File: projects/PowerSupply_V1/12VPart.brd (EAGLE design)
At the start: 50 x 50 mm, 26 parts, among them IC1 LM2596T, IC2 LM2596T, X1 IN, X2 OUT

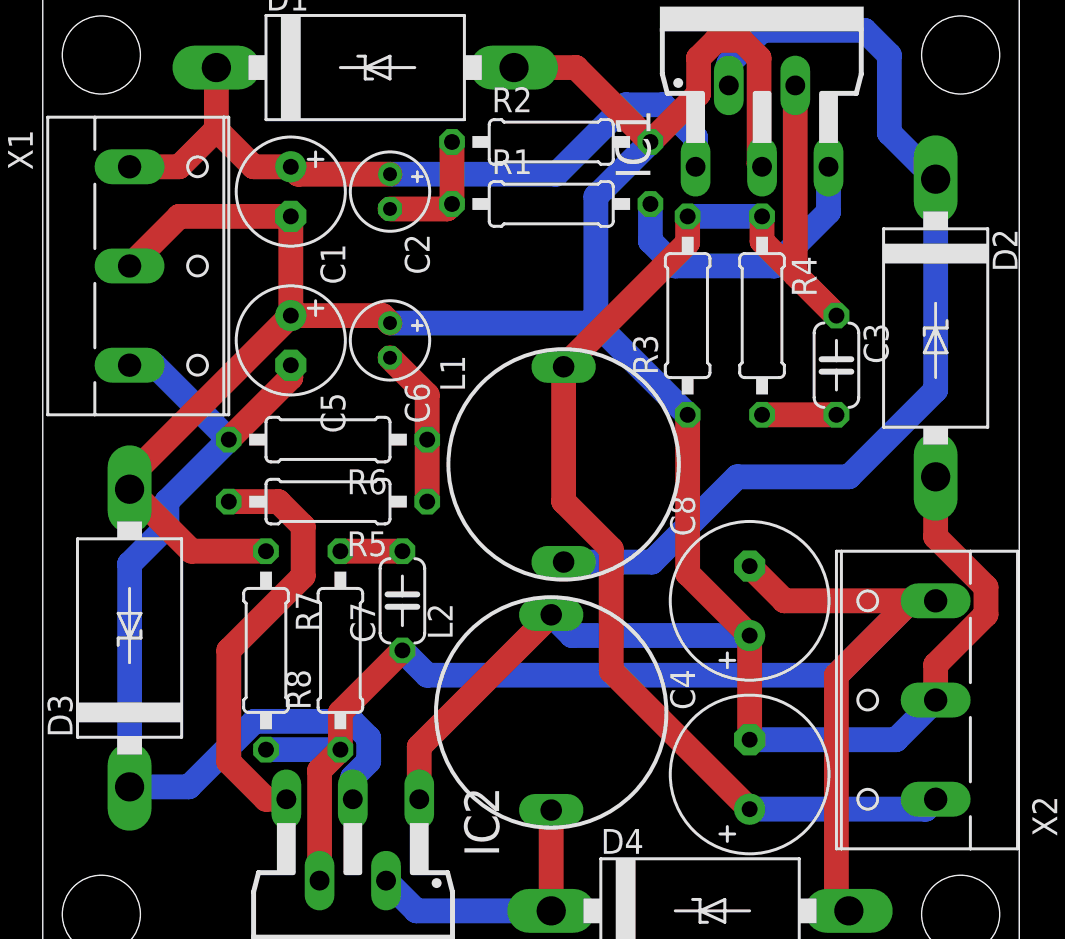
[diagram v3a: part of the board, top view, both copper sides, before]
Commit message: feat: 12VPart refactored
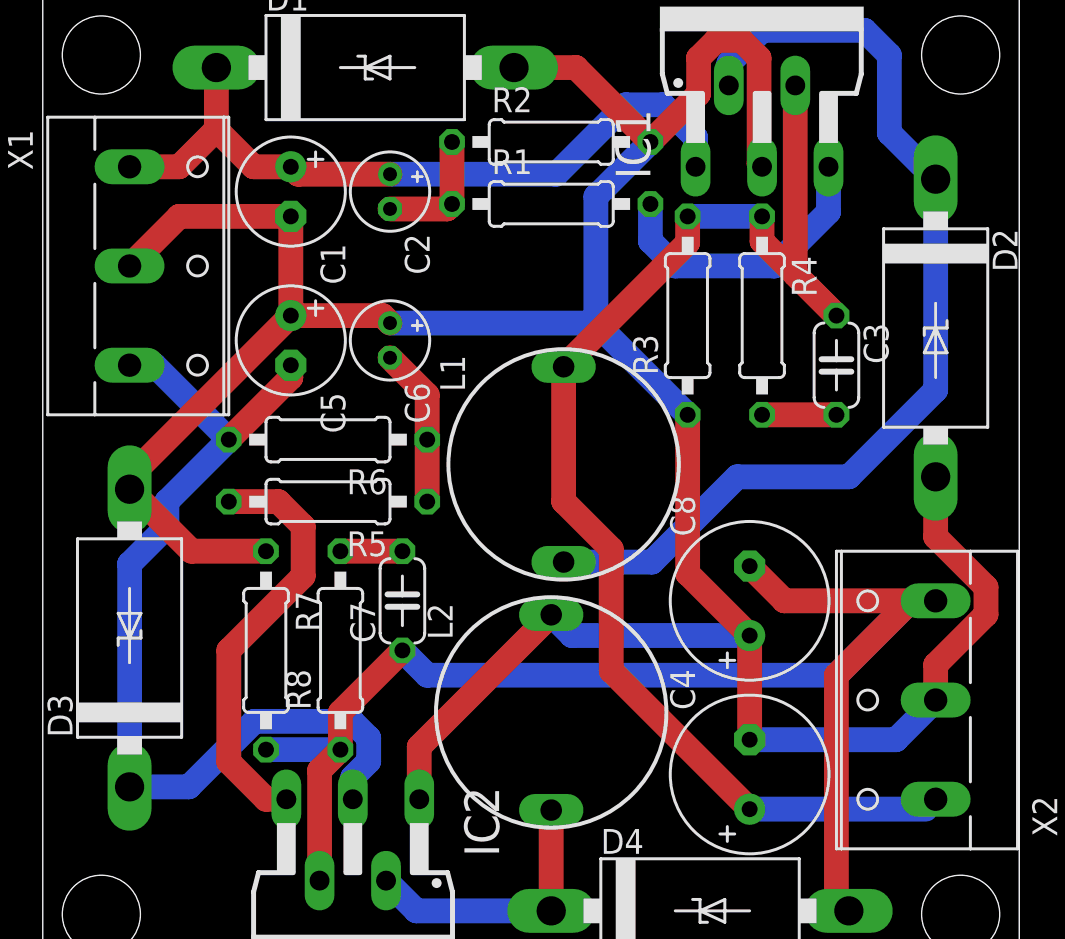
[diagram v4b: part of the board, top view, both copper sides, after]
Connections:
- net +24V renamed +20V
- net -24V renamed -20V
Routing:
- net -12V: track 76.0 -> 74.7 mm
- net +12V: track 69.8 -> 69.1 mm
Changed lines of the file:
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@@
 <wire x1="36.83" y1="28.575" x2="40.64" y2="28.575" width="1.27" layer="1"/>
-</signal>
-<signal name="+24V">
-<contactref element="X1" pad="1"/>
-<contactref element="C1" pad="+"/>
-<contactref element="IC1" pad="1"/>
-<contactref element="C2" pad="+"/>
-<contactref element="D1" pad="C"/>
-<wire x1="8.89" y1="45.72" x2="8.89" y2="46.355" width="1.27" layer="1"/>
-<wire x1="8.89" y1="43.18" x2="10.795" y2="41.275" width="1.27" layer="1"/>
-<wire x1="10.795" y1="41.275" x2="12.7" y2="41.275" width="1.27" layer="1"/>
-<wire x1="8.89" y1="46.355" x2="8.89" y2="43.18" width="1.27" layer="1"/>
-<wire x1="4.445" y1="41.275" x2="6.985" y2="41.275" width="1.27" layer="1"/>
-<wire x1="6.985" y1="41.275" x2="8.89" y2="43.18" width="1.27" layer="1"/>
-<wire x1="17.78" y1="40.894" x2="13.081" y2="40.894" width="1.27" layer="1"/>
-<wire x1="13.081" y1="40.894" x2="12.7" y2="41.275" width="1.27" layer="1"/>
-<wire x1="17.78" y1="40.894" x2="26.289" y2="40.894" width="1.27" layer="16"/>
-<wire x1="26.289" y1="40.894" x2="29.845" y2="44.45" width="1.27" layer="16"/>
-<wire x1="29.845" y1="44.45" x2="31.75" y2="44.45" width="1.27" layer="16"/>
-<wire x1="31.75" y1="44.45" x2="33.4264" y2="42.7736" width="1.27" layer="16"/>
-<wire x1="33.4264" y1="42.7736" x2="33.4264" y2="41.275" width="1.27" layer="16"/>
-</signal>
-<signal name="-24V">
-<contactref element="C5" pad="-"/>
-<contactref element="R6" pad="2"/>
-<contactref element="IC2" pad="3"/>
-<contactref element="D3" pad="C"/>
-<contactref element="X1" pad="3"/>
-<wire x1="9.525" y1="27.305" x2="12.7" y2="30.48" width="1.27" layer="1"/>
-<wire x1="12.7" y1="30.48" x2="12.7" y2="31.115" width="1.27" layer="1"/>
-<wire x1="16.6878" y1="10.8303" x2="16.6878" y2="12.0297" width="1.27" layer="16"/>
-<wire x1="16.6878" y1="12.0297" x2="15.8397" y2="12.8778" width="1.27" layer="16"/>
-<wire x1="7.4775" y1="9.525" x2="4.445" y2="9.525" width="1.27" layer="16"/>
-<wire x1="15.8397" y1="12.8778" x2="10.8303" y2="12.8778" width="1.27" layer="16"/>
-<wire x1="10.8303" y1="12.8778" x2="7.4775" y2="9.525" width="1.27" layer="16"/>
-<wire x1="15.875" y1="8.89" x2="15.875" y2="10.0175" width="1.27" layer="16"/>
-<wire x1="15.875" y1="10.0175" x2="16.6878" y2="10.8303" width="1.27" layer="16"/>
-<wire x1="4.445" y1="31.115" x2="5.715" y2="31.115" width="1.27" layer="16"/>
-<wire x1="5.715" y1="31.115" x2="9.525" y2="27.305" width="1.27" layer="16"/>
-<wire x1="9.525" y1="27.305" x2="6.35635" y2="24.13635" width="1.27" layer="16"/>
-<wire x1="6.35635" y1="24.13635" x2="6.35635" y2="22.8493375" width="1.27" layer="16"/>
-<wire x1="4.445" y1="20.9379875" x2="4.445" y2="9.525" width="1.27" layer="16"/>
-<wire x1="6.35635" y1="22.8493375" x2="4.445" y2="20.9379875" width="1.27" layer="16"/>
 </signal>
 <signal name="N$4">
@@
 <wire x1="19.685" y1="29.591" x2="19.685" y2="27.305" width="1.27" layer="1"/>
 </signal>
+<signal name="+20V">
+<contactref element="X1" pad="1"/>
+<contactref element="C1" pad="+"/>
+<contactref element="IC1" pad="1"/>
+<contactref element="C2" pad="+"/>
+<contactref element="D1" pad="C"/>
+<wire x1="8.89" y1="45.72" x2="8.89" y2="46.355" width="1.27" layer="1"/>
+<wire x1="8.89" y1="43.18" x2="10.795" y2="41.275" width="1.27" layer="1"/>
+<wire x1="10.795" y1="41.275" x2="12.7" y2="41.275" width="1.27" layer="1"/>
+<wire x1="8.89" y1="46.355" x2="8.89" y2="43.18" width="1.27" layer="1"/>
+<wire x1="8.89" y1="43.18" x2="6.985" y2="41.275" width="1.27" layer="1"/>
+<wire x1="17.78" y1="40.894" x2="13.081" y2="40.894" width="1.27" layer="1"/>
+<wire x1="13.081" y1="40.894" x2="12.7" y2="41.275" width="1.27" layer="1"/>
+<wire x1="17.78" y1="40.894" x2="26.289" y2="40.894" width="1.27" layer="16"/>
+<wire x1="26.289" y1="40.894" x2="29.845" y2="44.45" width="1.27" layer="16"/>
+<wire x1="29.845" y1="44.45" x2="31.75" y2="44.45" width="1.27" layer="16"/>
+<wire x1="31.75" y1="44.45" x2="33.4264" y2="42.7736" width="1.27" layer="16"/>
+<wire x1="33.4264" y1="42.7736" x2="33.4264" y2="41.275" width="1.27" layer="16"/>
+<wire x1="6.985" y1="41.275" x2="4.445" y2="41.275" width="1.27" layer="1"/>
+</signal>
+<signal name="-20V">
+<contactref element="X1" pad="3"/>
+<contactref element="D3" pad="C"/>
+<wire x1="16.6878" y1="10.8303" x2="16.6878" y2="12.0297" width="1.27" layer="16"/>
+<wire x1="16.6878" y1="12.0297" x2="15.8397" y2="12.8778" width="1.27" layer="16"/>
+<wire x1="7.4775" y1="9.525" x2="4.445" y2="9.525" width="1.27" layer="16"/>
+<wire x1="15.8397" y1="12.8778" x2="10.8303" y2="12.8778" width="1.27" layer="16"/>
+<wire x1="10.8303" y1="12.8778" x2="7.4775" y2="9.525" width="1.27" layer="16"/>
+<wire x1="15.875" y1="10.0175" x2="16.6878" y2="10.8303" width="1.27" layer="16"/>
+<wire x1="6.35635" y1="22.8493375" x2="6.35635" y2="24.13635" width="1.27" layer="16"/>
+<wire x1="4.445" y1="20.9379875" x2="4.445" y2="9.525" width="1.27" layer="16"/>
+<wire x1="6.35635" y1="22.8493375" x2="4.445" y2="20.9379875" width="1.27" layer="16"/>
+<contactref element="C5" pad="-"/>
+<contactref element="R6" pad="2"/>
+<contactref element="IC2" pad="3"/>
+<wire x1="12.7" y1="30.48" x2="9.525" y2="27.305" width="1.27" layer="1"/>
+<wire x1="5.715" y1="31.115" x2="9.525" y2="27.305" width="1.27" layer="16"/>
+<wire x1="6.35635" y1="24.13635" x2="9.525" y2="27.305" width="1.27" layer="16"/>
+<wire x1="12.7" y1="31.115" x2="12.7" y2="30.48" width="1.27" layer="1"/>
+<wire x1="15.875" y1="8.89" x2="15.875" y2="10.0175" width="1.27" layer="16"/>
+<wire x1="4.445" y1="31.115" x2="5.715" y2="31.115" width="1.27" layer="16"/>
+</signal>
 <signal name="+12V">
 <contactref element="X2" pad="1"/>
@@
 <wire x1="45.212" y1="8.382" x2="36.195" y2="8.382" width="1.27" layer="16"/>
 <wire x1="33.02" y1="38.735" x2="36.83" y2="38.735" width="1.27" layer="16"/>
-<wire x1="45.72" y1="8.89" x2="45.212" y2="8.382" width="1.27" layer="16"/>
+<wire x1="45.212" y1="8.382" x2="45.72" y2="8.89" width="0" layer="19" extent="16-16"/>
 </signal>
 <signal name="-12V">
@@
 <wire x1="11.43" y1="11.43" x2="15.24" y2="11.43" width="1.27" layer="16"/>
 <wire x1="18.415" y1="16.51" x2="19.685" y2="15.24" width="1.27" layer="16"/>
-<wire x1="37.973" y1="19.05" x2="36.195" y2="20.828" width="1.27" layer="1"/>
-<wire x1="40.64" y1="15.24" x2="44.45" y2="19.05" width="1.27" layer="16"/>
-<wire x1="44.45" y1="19.05" x2="45.72" y2="19.05" width="1.27" layer="16"/>
+<wire x1="36.195" y1="20.828" x2="37.973" y2="19.05" width="1.27" layer="1"/>
+<wire x1="44.45" y1="19.05" x2="40.64" y2="15.24" width="1.27" layer="16"/>
 <wire x1="19.685" y1="15.24" x2="40.64" y2="15.24" width="1.27" layer="16"/>
-<wire x1="45.72" y1="19.05" x2="37.973" y2="19.05" width="1.27" layer="1"/>
 <wire x1="41.275" y1="3.175" x2="40.64" y2="3.81" width="1.27" layer="1"/>
 <wire x1="40.64" y1="3.81" x2="40.64" y2="15.24" width="1.27" layer="1"/>
+<wire x1="37.973" y1="19.05" x2="44.45" y2="19.05" width="1.27" layer="1"/>
+<wire x1="44.45" y1="19.05" x2="45.72" y2="19.05" width="1.27" layer="1"/>
+<wire x1="45.72" y1="19.05" x2="44.45" y2="19.05" width="1.27" layer="16"/>
 <wire x1="40.64" y1="15.24" x2="44.45" y2="19.05" width="1.27" layer="1"/>
-<wire x1="44.45" y1="19.05" x2="45.72" y2="19.05" width="1.27" layer="1"/>
 </signal>
 </signals>

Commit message: feat: small fixes and changes applied
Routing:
- net +12V: track 69.1 -> 69.8 mm
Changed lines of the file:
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@@
 </element>
 <element name="D2" library="diode" library_urn="urn:adsk.eagle:library:210" package="C4111-15" package3d_urn="urn:adsk.eagle:package:43355/2" value="1N5822" x="45.72" y="33.02" smashed="yes" rot="R270">
-<attribute name="NAME" x="48.641" y="38.1" size="1.27" layer="25" ratio="10" rot="R270"/>
+<attribute name="NAME" x="47.371" y="40.64" size="1.27" layer="25" ratio="10" rot="R270"/>
 <attribute name="POPULARITY" value="0" x="16.51" y="-12.7" size="1.778" layer="27" rot="R270" display="off"/>
 <attribute name="VALUE" x="43.561" y="35.56" size="1.27" layer="27" ratio="10" rot="R270"/>
@@
 </element>
 <element name="D1" library="diode" library_urn="urn:adsk.eagle:library:210" package="C4111-15" package3d_urn="urn:adsk.eagle:package:43355/2" value="1N5822" x="16.51" y="46.355" smashed="yes">
-<attribute name="NAME" x="11.43" y="49.276" size="1.27" layer="25" ratio="10"/>
+<attribute name="NAME" x="8.89" y="48.006" size="1.27" layer="25" ratio="10"/>
 <attribute name="POPULARITY" value="0" x="59.69" y="8.255" size="1.778" layer="27" display="off"/>
 <attribute name="VALUE" x="13.97" y="44.196" size="1.27" layer="27" ratio="10"/>
@@
 <attribute name="OC_NEWARK" value="65K5910" x="83.82" y="38.735" size="1.778" layer="27" display="off"/>
 <attribute name="POPULARITY" value="0" x="83.82" y="38.735" size="1.778" layer="27" display="off"/>
-<attribute name="VALUE" x="44.45" y="40.64" size="1.778" layer="27" ratio="10" rot="R90"/>
+<attribute name="VALUE" x="21.59" y="47.625" size="1.778" layer="27" ratio="10"/>
 </element>
 <element name="IC2" library="national-semiconductor" library_urn="urn:adsk.eagle:library:307" package="T05D" package3d_urn="urn:adsk.eagle:package:21216/1" value="LM2596T" x="15.875" y="3.81" smashed="yes" rot="R180">
 <attribute name="MF" value="" x="-5.715" y="24.13" size="1.778" layer="27" rot="R180" display="off"/>
 <attribute name="MPN" value="LM2596T-ADJ/LF02" x="-5.715" y="24.13" size="1.778" layer="27" rot="R180" display="off"/>
-<attribute name="NAME" x="21.59" y="9.525" size="1.778" layer="25" ratio="10" rot="R270"/>
+<attribute name="NAME" x="20.32" y="5.715" size="1.778" layer="25" ratio="10"/>
 <attribute name="OC_FARNELL" value="9494162" x="-5.715" y="24.13" size="1.778" layer="27" rot="R180" display="off"/>
 <attribute name="OC_NEWARK" value="65K5910" x="-5.715" y="24.13" size="1.778" layer="27" rot="R180" display="off"/>
 <attribute name="POPULARITY" value="0" x="-5.715" y="24.13" size="1.778" layer="27" rot="R180" display="off"/>
-<attribute name="VALUE" x="8.255" y="9.525" size="1.778" layer="27" ratio="10" rot="R270"/>
+<attribute name="VALUE" x="0.635" y="5.08" size="1.778" layer="27" ratio="10"/>
 </element>
 <element name="L1" library="inductor-neosid" library_urn="urn:adsk.eagle:library:241" package="SD12-680" package3d_urn="urn:adsk.eagle:package:14657/1" value="33µH" x="26.67" y="26.035" smashed="yes" rot="R90">
 <attribute name="MF" value="BUSSMANN" x="33.02" y="45.085" size="1.778" layer="27" rot="R90" display="off"/>
 <attribute name="MPN" value="SD12-680" x="33.02" y="45.085" size="1.778" layer="27" rot="R90" display="off"/>
-<attribute name="NAME" x="21.622" y="29.762" size="1.27" layer="25" rot="R90"/>
+<attribute name="NAME" x="24.797" y="25.317" size="1.27" layer="25" rot="R90"/>
 <attribute name="OC_FARNELL" value="unknown" x="33.02" y="45.085" size="1.778" layer="27" rot="R90" display="off"/>
 <attribute name="OC_NEWARK" value="19K7201" x="33.02" y="45.085" size="1.778" layer="27" rot="R90" display="off"/>
 <attribute name="POPULARITY" value="0" x="33.02" y="45.085" size="1.778" layer="27" rot="R90" display="off"/>
-<attribute name="VALUE" x="29.67" y="22.785" size="1.27" layer="27" rot="R90"/>
+<attribute name="VALUE" x="29.67" y="24.055" size="1.27" layer="27" rot="R90"/>
 </element>
 <element name="L2" library="inductor-neosid" library_urn="urn:adsk.eagle:library:241" package="SD12-680" package3d_urn="urn:adsk.eagle:package:14657/1" value="47µH" x="26.035" y="13.335" smashed="yes" rot="R90">
 <attribute name="MF" value="BUSSMANN" x="32.385" y="45.085" size="1.778" layer="27" rot="R90" display="off"/>
 <attribute name="MPN" value="SD12-680" x="32.385" y="45.085" size="1.778" layer="27" rot="R90" display="off"/>
-<attribute name="NAME" x="20.987" y="17.062" size="1.27" layer="25" rot="R90"/>
+<attribute name="NAME" x="24.162" y="12.617" size="1.27" layer="25" rot="R90"/>
 <attribute name="OC_FARNELL" value="unknown" x="32.385" y="45.085" size="1.778" layer="27" rot="R90" display="off"/>
 <attribute name="OC_NEWARK" value="19K7201" x="32.385" y="45.085" size="1.778" layer="27" rot="R90" display="off"/>
@@
 <attribute name="MF" value="" x="-16.51" y="-1.905" size="1.778" layer="27" rot="R270" display="off"/>
 <attribute name="MPN" value="" x="-16.51" y="-1.905" size="1.778" layer="27" rot="R270" display="off"/>
-<attribute name="NAME" x="-1.778" y="43.18" size="1.27" layer="25" ratio="10" rot="R270"/>
+<attribute name="NAME" x="0.762" y="31.115" size="1.27" layer="25" ratio="10" rot="R270"/>
 <attribute name="OC_FARNELL" value="unknown" x="-16.51" y="-1.905" size="1.778" layer="27" rot="R270" display="off"/>
 <attribute name="OC_NEWARK" value="unknown" x="-16.51" y="-1.905" size="1.778" layer="27" rot="R270" display="off"/>
 <attribute name="POPULARITY" value="3" x="-16.51" y="-1.905" size="1.778" layer="27" rot="R270" display="off"/>
-<attribute name="VALUE" x="0.762" y="42.799" size="1.27" layer="27" ratio="10" rot="R270"/>
+<attribute name="VALUE" x="0.762" y="43.434" size="1.27" layer="27" ratio="10" rot="R270"/>
 </element>
 <element name="X2" library="con-wago-508" library_urn="urn:adsk.eagle:library:196" package="W237-133" package3d_urn="urn:adsk.eagle:package:10737/1" value="OUT" x="45.085" y="13.97" smashed="yes" rot="R90">
 <attribute name="MF" value="" x="66.675" y="68.58" size="1.778" layer="27" rot="R90" display="off"/>
 <attribute name="MPN" value="" x="66.675" y="68.58" size="1.778" layer="27" rot="R90" display="off"/>
-<attribute name="NAME" x="51.943" y="6.985" size="1.27" layer="25" ratio="10" rot="R90"/>
+<attribute name="NAME" x="49.403" y="19.05" size="1.27" layer="25" ratio="10" rot="R90"/>
 <attribute name="OC_FARNELL" value="unknown" x="66.675" y="68.58" size="1.778" layer="27" rot="R90" display="off"/>
 <attribute name="OC_NEWARK" value="unknown" x="66.675" y="68.58" size="1.778" layer="27" rot="R90" display="off"/>
 <attribute name="POPULARITY" value="3" x="66.675" y="68.58" size="1.778" layer="27" rot="R90" display="off"/>
-<attribute name="VALUE" x="49.403" y="7.366" size="1.27" layer="27" ratio="10" rot="R90"/>
+<attribute name="VALUE" x="49.403" y="6.731" size="1.27" layer="27" ratio="10" rot="R90"/>
 </element>
 </elements>
@@
 <wire x1="45.212" y1="8.382" x2="36.195" y2="8.382" width="1.27" layer="16"/>
 <wire x1="33.02" y1="38.735" x2="36.83" y2="38.735" width="1.27" layer="16"/>
-<wire x1="45.212" y1="8.382" x2="45.72" y2="8.89" width="0" layer="19" extent="16-16"/>
+<wire x1="45.72" y1="8.89" x2="45.212" y2="8.382" width="1.27" layer="16"/>
 </signal>
 <signal name="-12V">
